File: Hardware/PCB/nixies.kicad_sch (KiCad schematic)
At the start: 28 parts, among them J10 Sec_One, J3 Hr_Ten, J4 Hr_One, J5 Min_dot, J6 Min_Ten, J7 Min_One, J8 Sec_Dot, J9 Sec_Ten

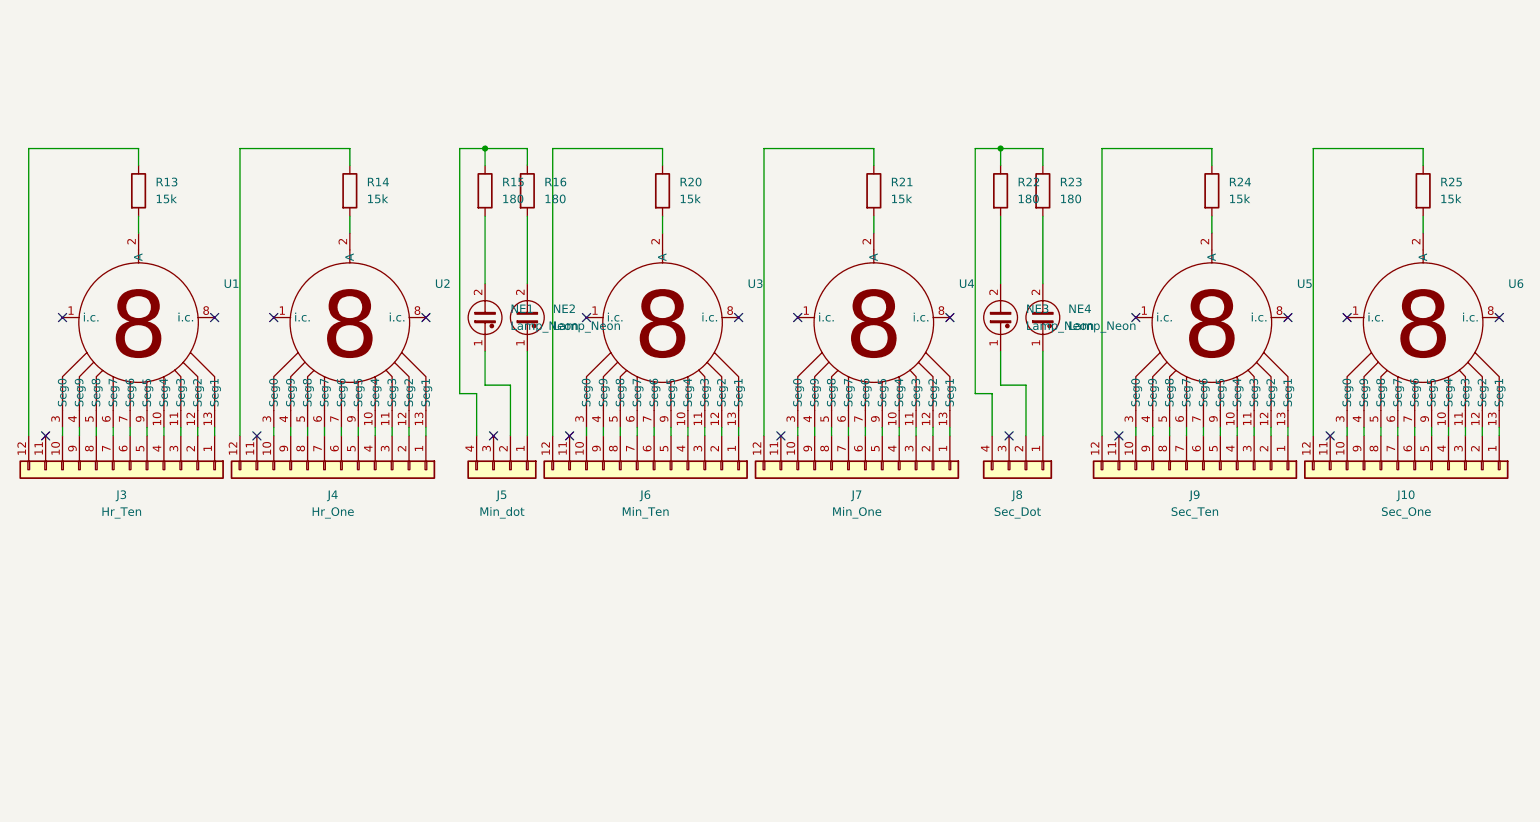
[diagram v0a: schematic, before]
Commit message: schematic update
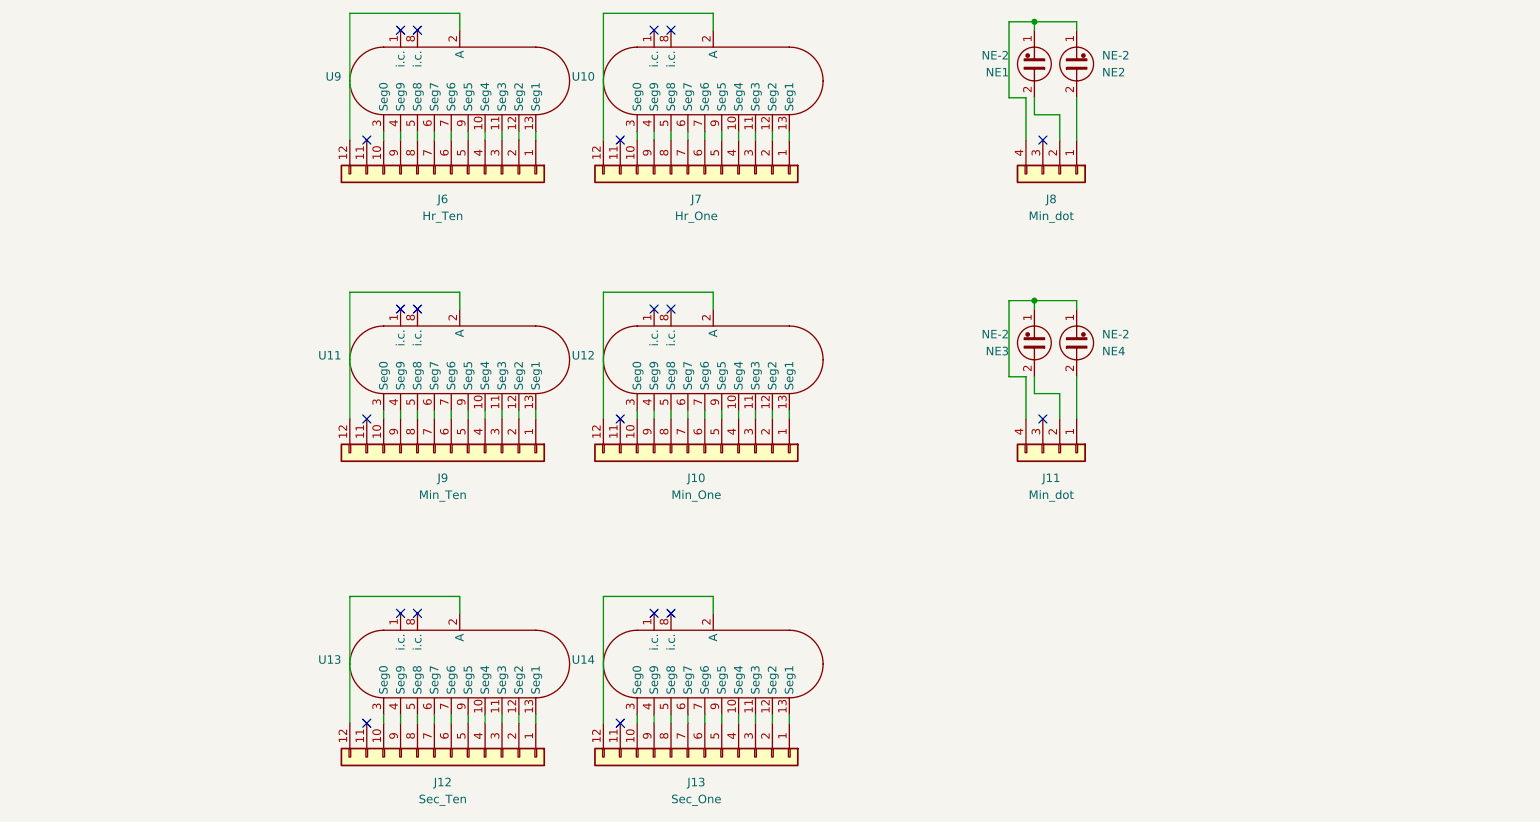
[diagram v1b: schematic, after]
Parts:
- removed J8: Sec_Dot, symbol Connector_Generic:Conn_01x04
- removed R13, R14, R20, R21, R24, R25: 15k, symbol Device:R
- removed R15, R16, R22, R23: 180, symbol Device:R
- removed U1, U2, U3, U4, U5, U6: ~, symbol Eigene:Z5600M
- added J11: Min_dot, symbol Connector_Generic:Conn_01x04
- added U10, U11, U12, U13, U14, U9: ~, symbol Eigene:Z5600M
- NE1, NE2, NE3, NE4: value Lamp_Neon -> NE-2
- renumbered J7 to J10, J9 to J12, J10 to J13, J3 to J6, J4 to J7, J5 to J8, J6 to J9
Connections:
- net at J9.4 (Pin_4): now also U11.10 (Seg4)
- net at J9.3 (Pin_3): now also U11.11 (Seg3)
- net at J9.2 (Pin_2): now also U11.12 (Seg2)
- net at J9.1 (Pin_1): now also U11.13 (Seg1)
- net at J9.10 (Pin_10): now also U11.3 (Seg0)
- net at J9.9 (Pin_9): now also U11.4 (Seg9)
- net at J9.8 (Pin_8): now also U11.5 (Seg8)
- net at J9.7 (Pin_7): now also U11.6 (Seg7)
- net at J9.6 (Pin_6): now also U11.7 (Seg6)
- net at J9.5 (Pin_5): now also U11.9 (Seg5)
- net at NE2.1: now also J8.4 (Pin_4), NE1.1; no longer J8.1 (Pin_1)
- net at NE2.2: now also J8.1 (Pin_1)
- net at NE4.1: now also NE3.1, J11.4 (Pin_4)
- net at J13.12 (Pin_12): now also U14.2 (A)
- net at J8.2 (Pin_2): now also NE1.2; no longer NE1.1
- net at J7.12 (Pin_12): now also U10.2 (A)
- net at J6.12 (Pin_12): now also U9.2 (A)
- net at NE3.2: now also J11.2 (Pin_2)
- net at J7.1 (Pin_1): now also U10.13 (Seg1)
- net at J7.10 (Pin_10): now also U10.3 (Seg0)
- net at J7.2 (Pin_2): now also U10.12 (Seg2)
- net at J7.3 (Pin_3): now also U10.11 (Seg3)
- net at J7.4 (Pin_4): now also U10.10 (Seg4)
- net at J7.5 (Pin_5): now also U10.9 (Seg5)
- net at J7.6 (Pin_6): now also U10.7 (Seg6)
- net at J7.7 (Pin_7): now also U10.6 (Seg7)
- net at J7.8 (Pin_8): now also U10.5 (Seg8)
- net at J7.9 (Pin_9): now also U10.4 (Seg9)
- net at J6.1 (Pin_1): now also U9.13 (Seg1)
- net at J6.10 (Pin_10): now also U9.3 (Seg0)
- net at J6.2 (Pin_2): now also U9.12 (Seg2)
- net at J6.3 (Pin_3): now also U9.11 (Seg3)
- net at J6.4 (Pin_4): now also U9.10 (Seg4)
- net at J6.5 (Pin_5): now also U9.9 (Seg5)
- net at J6.6 (Pin_6): now also U9.7 (Seg6)
- net at J6.7 (Pin_7): now also U9.6 (Seg7)
- net at J6.8 (Pin_8): now also U9.5 (Seg8)
- net at J6.9 (Pin_9): now also U9.4 (Seg9)
- net at J12.12 (Pin_12): now also U13.2 (A)
- net at J12.1 (Pin_1): now also U13.13 (Seg1)
- net at J12.10 (Pin_10): now also U13.3 (Seg0)
- net at J12.2 (Pin_2): now also U13.12 (Seg2)
- net at J12.3 (Pin_3): now also U13.11 (Seg3)
- net at J12.4 (Pin_4): now also U13.10 (Seg4)
- net at J12.5 (Pin_5): now also U13.9 (Seg5)
- net at J12.6 (Pin_6): now also U13.7 (Seg6)
- net at J12.7 (Pin_7): now also U13.6 (Seg7)
- net at J12.8 (Pin_8): now also U13.5 (Seg8)
- net at J12.9 (Pin_9): now also U13.4 (Seg9)
- net at J10.4 (Pin_4): now also U12.10 (Seg4)
- net at J10.3 (Pin_3): now also U12.11 (Seg3)
- net at J10.2 (Pin_2): now also U12.12 (Seg2)
- net at J10.1 (Pin_1): now also U12.13 (Seg1)
- net at J10.10 (Pin_10): now also U12.3 (Seg0)
- net at J10.9 (Pin_9): now also U12.4 (Seg9)
- net at J10.8 (Pin_8): now also U12.5 (Seg8)
- net at J10.7 (Pin_7): now also U12.6 (Seg7)
- net at J10.6 (Pin_6): now also U12.7 (Seg6)
- net at J10.5 (Pin_5): now also U12.9 (Seg5)
- net at J10.12 (Pin_12): now also U12.2 (A)
- net at NE4.2: now also J11.1 (Pin_1)
- net at J13.1 (Pin_1): now also U14.13 (Seg1)
- net at J13.10 (Pin_10): now also U14.3 (Seg0)
- net at J13.2 (Pin_2): now also U14.12 (Seg2)
- net at J13.3 (Pin_3): now also U14.11 (Seg3)
- net at J13.4 (Pin_4): now also U14.10 (Seg4)
- net at J13.5 (Pin_5): now also U14.9 (Seg5)
- net at J13.6 (Pin_6): now also U14.7 (Seg6)
- net at J13.7 (Pin_7): now also U14.6 (Seg7)
- net at J13.8 (Pin_8): now also U14.5 (Seg8)
- net at J13.9 (Pin_9): now also U14.4 (Seg9)
- net at J9.12 (Pin_12): now also U11.2 (A)
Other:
- moved on the sheet: J10, J12, J13, J6, J7, J8, J9, NE1

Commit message: Hardware Update Schematic Done Placement started
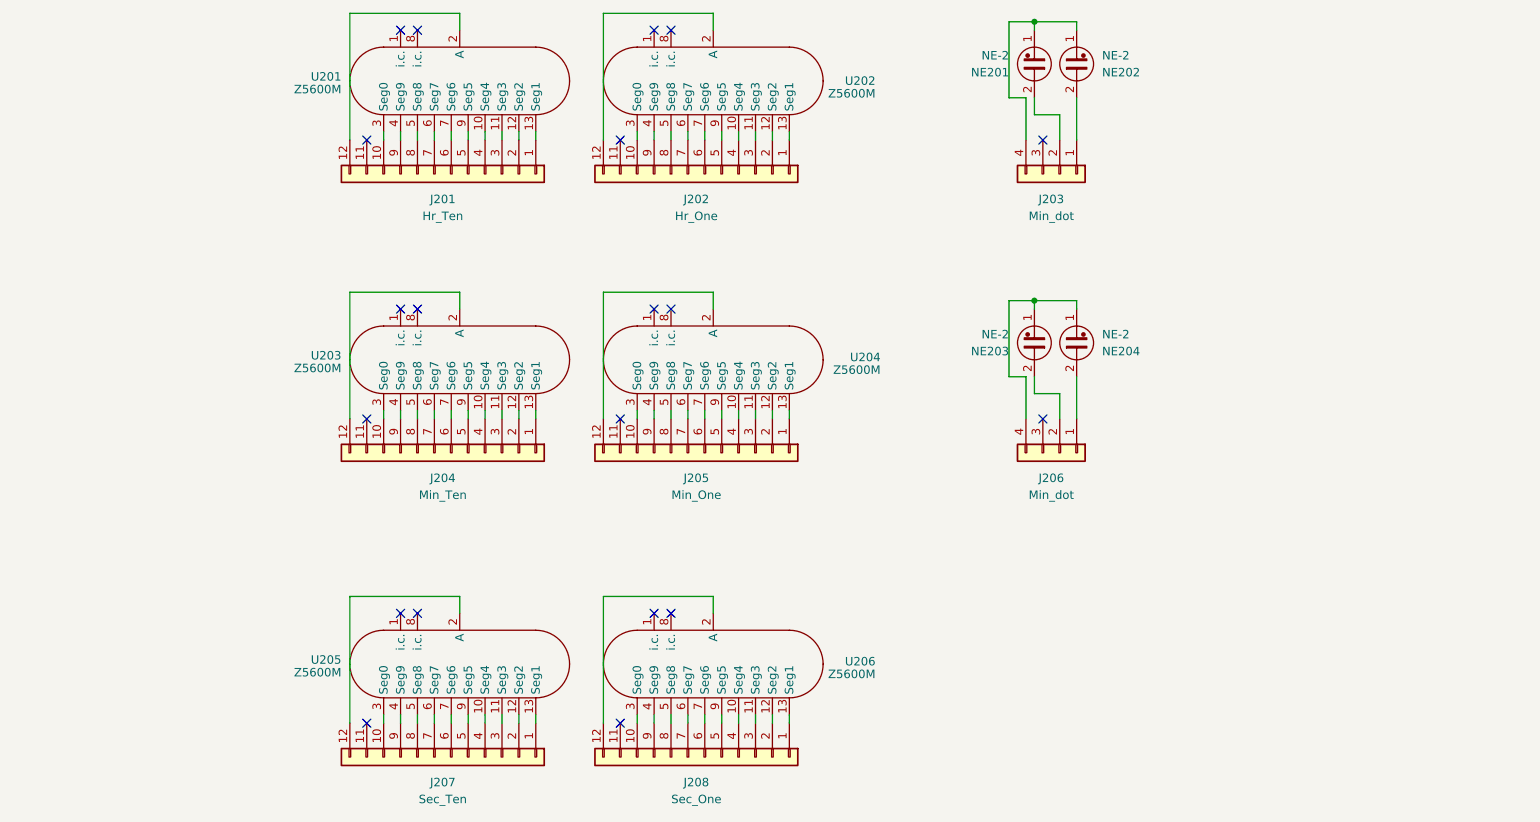
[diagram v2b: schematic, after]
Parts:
- J201: renamed from J6; footprint (none) -> Connector_PinSocket_2.54mm:PinSocket_1x12_P2.54mm_Vertical
- J202: renamed from J7; footprint (none) -> Connector_PinSocket_2.54mm:PinSocket_1x12_P2.54mm_Vertical
- J203: renamed from J8; footprint (none) -> Connector_PinSocket_2.54mm:PinSocket_1x04_P2.54mm_Vertical
- J204: renamed from J9; footprint (none) -> Connector_PinSocket_2.54mm:PinSocket_1x12_P2.54mm_Vertical
- J205: renamed from J10; footprint (none) -> Connector_PinSocket_2.54mm:PinSocket_1x12_P2.54mm_Vertical
- J206: renamed from J11; footprint (none) -> Connector_PinSocket_2.54mm:PinSocket_1x04_P2.54mm_Vertical
- J207: renamed from J12; footprint (none) -> Connector_PinSocket_2.54mm:PinSocket_1x12_P2.54mm_Vertical
- J208: renamed from J13; footprint (none) -> Connector_PinSocket_2.54mm:PinSocket_1x12_P2.54mm_Vertical
- NE201: renamed from NE1; footprint (none) -> Valve:Valve_Glimm
- NE202: renamed from NE2; footprint (none) -> Valve:Valve_Glimm
- NE203: renamed from NE3; footprint (none) -> Valve:Valve_Glimm
- NE204: renamed from NE4; footprint (none) -> Valve:Valve_Glimm
- U201: renamed from U9; value ~ -> Z5600M; footprint (none) -> Eigene:B13B
- U202: renamed from U10; value ~ -> Z5600M; footprint (none) -> Eigene:B13B
- U203: renamed from U11; value ~ -> Z5600M; footprint (none) -> Eigene:B13B
- U204: renamed from U12; value ~ -> Z5600M; footprint (none) -> Eigene:B13B
- U205: renamed from U13; value ~ -> Z5600M; footprint (none) -> Eigene:B13B
- U206: renamed from U14; value ~ -> Z5600M; footprint (none) -> Eigene:B13B
